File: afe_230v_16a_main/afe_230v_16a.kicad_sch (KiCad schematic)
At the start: 76 parts, among them J4 MCV 1,5/ 6-G-3,81, J5 HBUS16, J6 pinheader_2x6_socket, P1 06-14-03_rectifier, U1 ${SIM.PARAMS}, U17 1_element_2_current, U2 AD8538, U20 watt_hour_meter_bidirectional, U21 3w_ne, U3 AD8538_dnp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

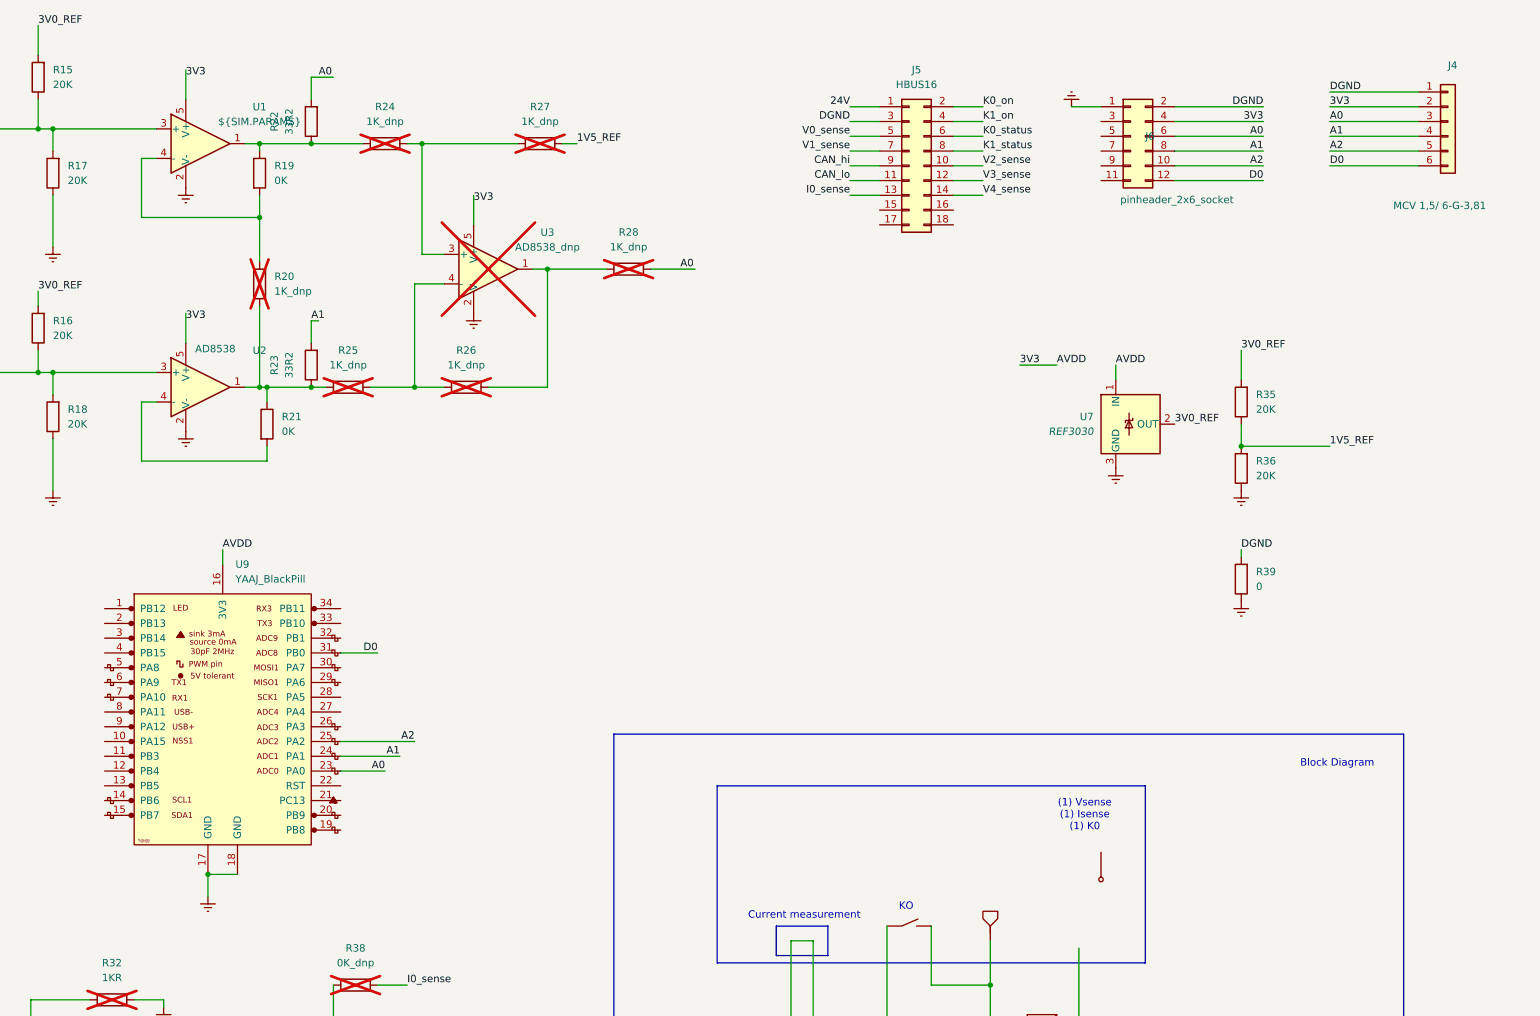
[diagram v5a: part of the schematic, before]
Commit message: changed BP footprint, added stlink connection, added 3d models
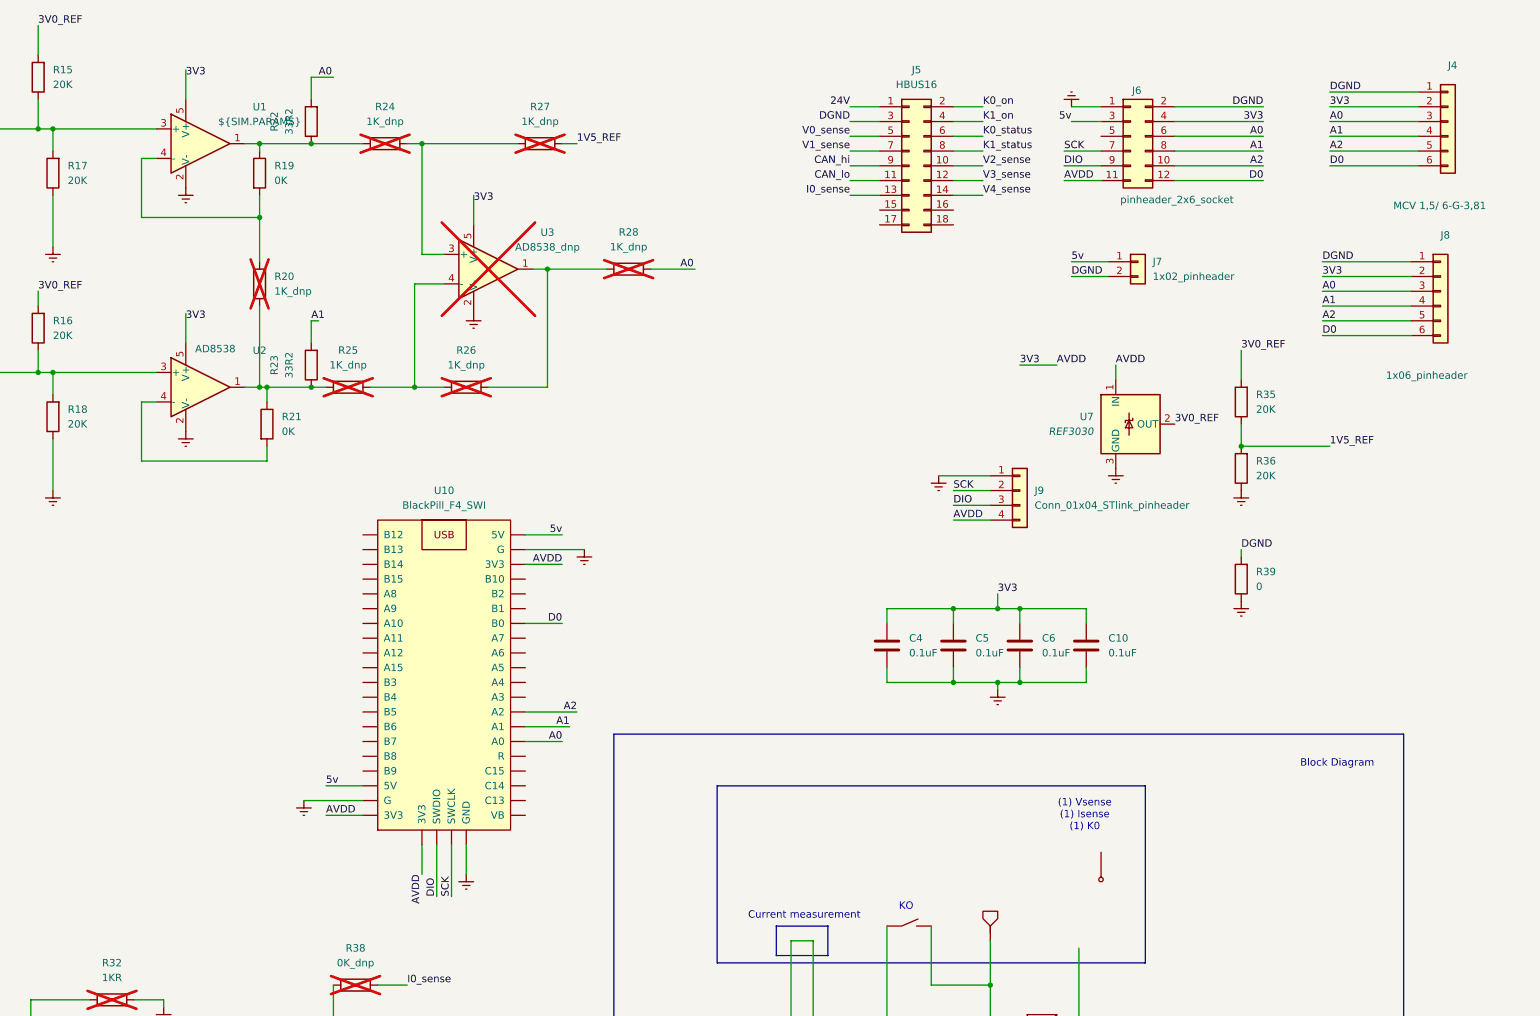
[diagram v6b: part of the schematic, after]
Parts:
- removed U9: YAAJ_BlackPill, STM-32:YAAJ_BlackPill_SWD_2, symbol YAAJ_BlackPill:YAAJ_BlackPill
- added C10, C4, C5, C6: 0.1uF, Capacitor_SMD:C_0603_1608Metric_Pad1.08x0.95mm_HandSolder, symbol Device:C
- added J7: 1x02_pinheader, Connector_PinHeader_2.54mm:PinHeader_1x02_P2.54mm_Vertical, symbol Connector_Generic:Conn_01x02
- added J8: 1x06_pinheader, Connector_PinHeader_2.54mm:PinHeader_1x06_P2.54mm_Vertical, symbol Connector_Generic:Conn_01x06
- added J9: Conn_01x04_STlink_pinheader, Connector_PinHeader_2.54mm:PinHeader_1x04_P2.54mm_Vertical, symbol Connector_Generic:Conn_01x04
- added U10: BlackPill_F4_SWI, MSZ_STM32:Blackpill_F4_SWI, symbol MSZ98_blackpill:BlackPill_F4_SWI
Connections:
- net 3V3: now also J6.11 (Pin_11), C10.1, C4.1, C5.1, C6.1, J8.2 (Pin_2), J9.4 (Pin_4), U10.20 (3V3), U10.38 (3V3), U10.41 (3V3)
- net A0: now also J8.3 (Pin_3), U10.26 (A0)
- net A1: now also J8.4 (Pin_4), U10.27 (A1)
- net A2: now also J8.5 (Pin_5), U10.28 (A2)
- net D0: now also J8.6 (Pin_6), U10.34 (B0)
- net DGND: now also J7.2 (Pin_2), J8.1 (Pin_1)
- net Earth: now also C10.2, C4.2, C5.2, C6.2, J9.1 (Pin_1), U10.19 (G), U10.39 (G), U10.44 (GND)
- net at U20.: now also T16.
- net at T16.: now also T17.; no longer U20.
- net 5v: now reaches J6.3 (Pin_3)
- net 5v: now also J7.1 (Pin_1), U10.18 (5V), U10.40 (5V)
- net SCK: now reaches J6.7 (Pin_7)
- net SCK: now also J9.2 (Pin_2), U10.43 (SWCLK)
- net DIO: now reaches J6.9 (Pin_9)
- net DIO: now also J9.3 (Pin_3), U10.42 (SWDIO)
- net at C8.: now also T10.
- net at T10.: now also T8.; no longer C8.
- net at C7.: now also C3., P1., T8., U8.
- net at T17.: now also C12.; no longer T16.
- net at T7.: now also C3.
- net at T11.: now also C9.; no longer T9.
- net at C9.: no longer T11.
- net at U21.: no longer C12.
- new net: T11., T9.
- new net: C12., U21.
- now unconnected: P1., U8.

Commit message: swapped connectors
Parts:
- removed J1, J2, J3: ~, Connector_Phoenix_MSTB:PhoenixContact_MSTBVA_2,5_2-G-5,08_1x02_P5.08mm_Vertical, symbol Connector_Generic:Conn_01x02
- removed J4: MCV 1,5/ 6-G-3,81, Connector_Phoenix_MC:PhoenixContact_MCV_1,5_6-G-3.81_1x06_P3.81mm_Vertical, symbol Connector_Generic:Conn_01x06
- removed J7: 1x02_pinheader, Connector_PinHeader_2.54mm:PinHeader_1x02_P2.54mm_Vertical, symbol Connector_Generic:Conn_01x02
- removed J8: 1x06_pinheader, Connector_PinHeader_2.54mm:PinHeader_1x06_P2.54mm_Vertical, symbol Connector_Generic:Conn_01x06
- added D5, D6: LED, LED_SMD:LED_0805_2012Metric, symbol Device:LED
- added J1: MKDSN 2,5/ 6-5,08, kyuditsky:1989405, symbol Connector_Generic:Conn_01x06
- added J2: MKDS 1,5/ 6, kyuditsky:1715190, symbol Connector_Generic:Conn_01x06
- added R40, R41: 2.2k, Resistor_SMD:R_0805_2012Metric, symbol Device:R
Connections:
- net 3V3: now also D6.2 (A), J2.2 (Pin_2)
- net 5v: now also D5.2 (A)
- net A0: now also J2.3 (Pin_3)
- net A1: now also J2.4 (Pin_4)
- net A2: now also J2.5 (Pin_5)
- net D0: now also J2.6 (Pin_6)
- net DGND: now also J6.5 (Pin_5), J9.1 (Pin_1), J2.1 (Pin_1)
- net Earth: now also R40.1, R41.1; no longer J9.1 (Pin_1)
- net I_n: now also J1.6 (Pin_6)
- net I_p: now also J1.5 (Pin_5)
- net K_i: now also J1.3 (Pin_3)
- net K_o: now also J1.4 (Pin_4)
- net V0_n: now also J1.2 (Pin_2)
- net V0_p: now also J1.1 (Pin_1)
- net at U20.: now also T16.
- net at T16.: now also T17.; no longer U20.
- net at C8.: now also T10.
- net at T10.: now also T8.; no longer C8.
- net at C7.: now also C3., P1., T8., U8.
- net at T17.: now also C12.; no longer T16.
- net at T7.: now also C3.
- net at T11.: now also C9.; no longer T9.
- net at C9.: no longer T11.
- net at U21.: no longer C12.
- new net: D5.1 (K), R40.2
- new net: T11., T9.
- new net: D6.1 (K), R41.2
- new net: C12., U21.
- now unconnected: P1., U8.
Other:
- moved on the sheet: J9

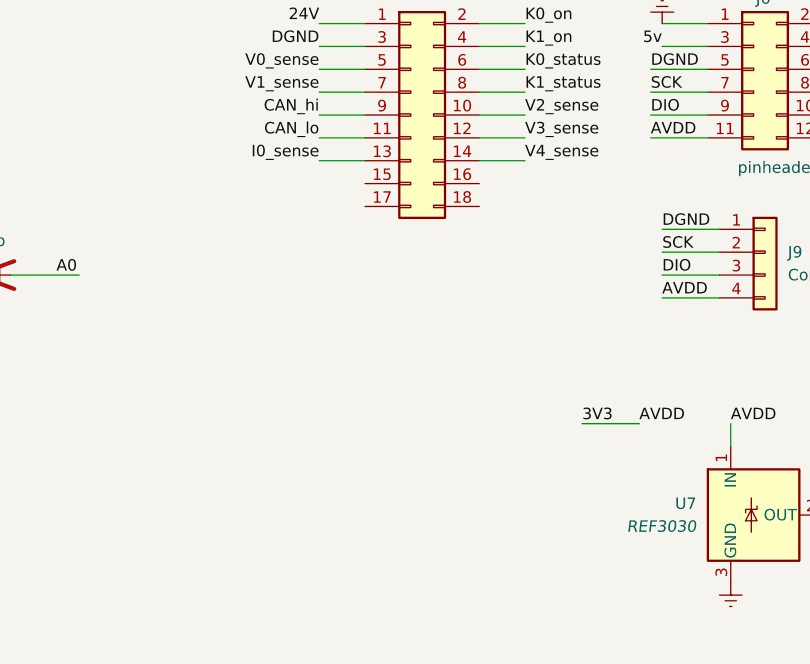
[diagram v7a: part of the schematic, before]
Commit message: added 15/16 0ohm resistors
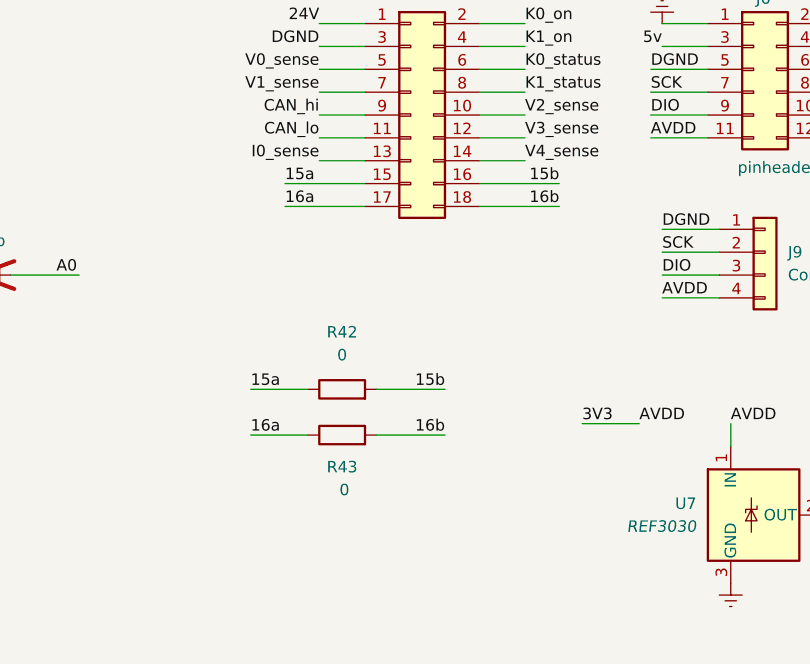
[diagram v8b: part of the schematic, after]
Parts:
- added R42, R43: 0, Resistor_SMD:R_0805_2012Metric, symbol Device:R
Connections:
- net at U20.: now also T16.
- net at T16.: now also T17.; no longer U20.
- net at C8.: now also T10.
- net at T10.: now also T8.; no longer C8.
- net 15a: now reaches J5.15 (Pin_15)
- net 15a: now also R42.1
- net 15b: now reaches J5.16 (Pin_16)
- net 15b: now also R42.2
- net 16a: now reaches J5.17 (Pin_17)
- net 16a: now also R43.1
- net 16b: now reaches J5.18 (Pin_18)
- net 16b: now also R43.2
- net at C7.: now also C3., P1., T8., U8.
- net at T17.: now also C12.; no longer T16.
- net at T7.: now also C3.
- net at T11.: now also C9.; no longer T9.
- net at C9.: no longer T11.
- net at U21.: no longer C12.
- new net: T11., T9.
- new net: C12., U21.
- now unconnected: P1., U8.
